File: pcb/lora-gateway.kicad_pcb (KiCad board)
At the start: 2 copper layers, 78.3 x 25.8 mm, 22 parts, among them J1 USB_B_Micro, J2 Conn_01x06, J3 Conn_01x06, J4 Conn_Coaxial, J5 AVR-JTAG-10, J6 AVR-ISP-6, SW1 SW_Push, U1 RFM95W-868S2, U2 ATmega2560-16A, U3 LM1117-3.3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

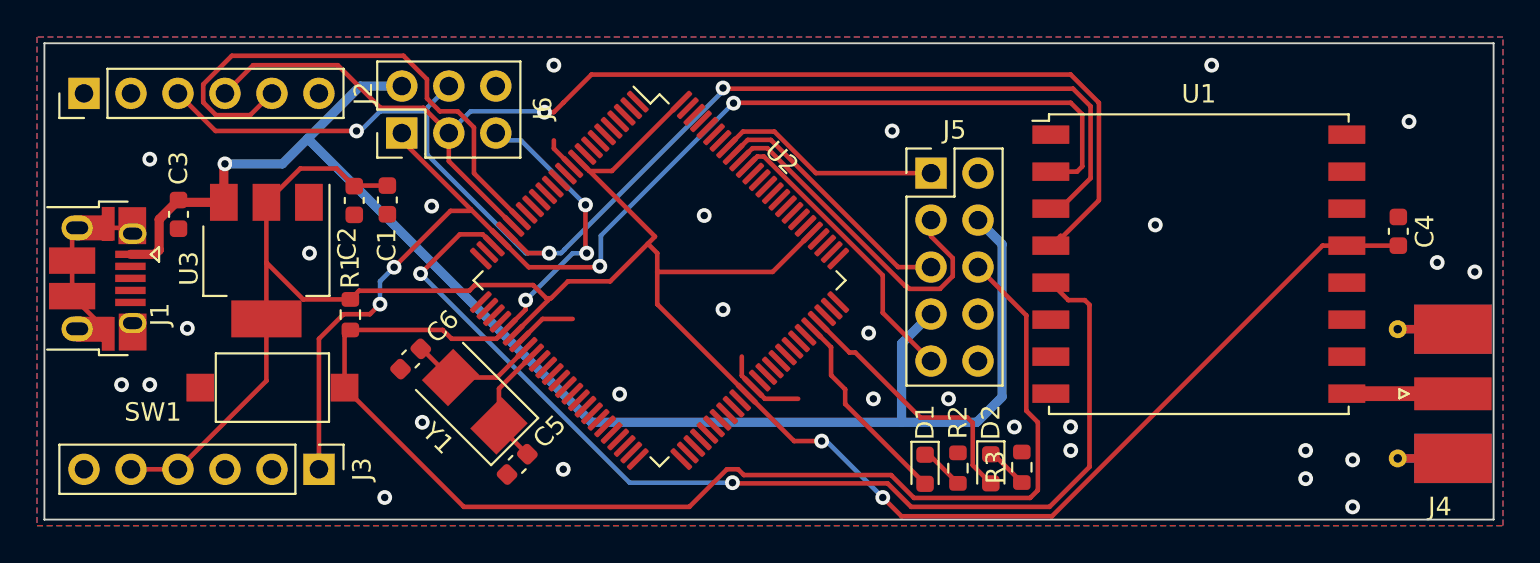
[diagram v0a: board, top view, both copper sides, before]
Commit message: add rfm95 wiring
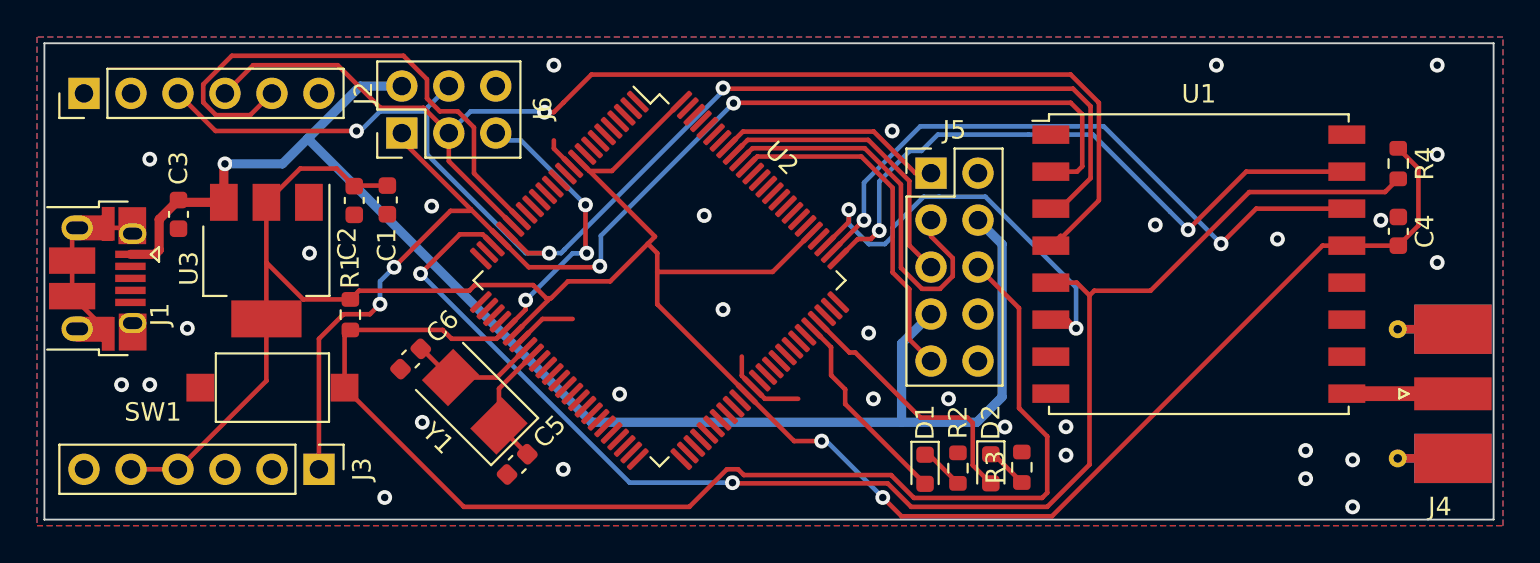
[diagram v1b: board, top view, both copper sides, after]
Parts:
- added R4: R_Small, Resistor_SMD:R_0603_1608Metric, F.Cu at (111.7, 64.8)
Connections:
- U1 pad 14: unconnected-(U1-DIO0-Pad14) -> DIO0
- U1 pad 15: unconnected-(U1-DIO1-Pad15) -> DIO1
- U2 pad 76: unconnected-(U2-PA2-Pad76) -> DIO1
- U2 pad 77: unconnected-(U2-PA1-Pad77) -> DIO0
- U2 pad 78: unconnected-(U2-PA0-Pad78) -> RST_LORA
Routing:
- net DIO0: track 0.00 -> 35.3 mm, vias 0 -> 2
- net DIO1: track 0.00 -> 35.3 mm, vias 0 -> 2
- net RST_LORA: track 0.00 -> 23.1 mm, vias 0 -> 2
- net SS_LORA: track 58.7 -> 78.2 mm
- net +3V3: track 129.2 -> 135.4 mm
- net TDI: track 16.0 -> 19.0 mm
- net TDO: track 18.7 -> 21.4 mm
- net TMS: track 13.8 -> 15.9 mm
- net RST: track 82.7 -> 83.5 mm
- net GND: vias 29 -> 31

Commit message: add gnd to micro usb
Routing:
- net GND: track 9.80 -> 12.2 mm
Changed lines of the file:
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@@
   (segment (start 66.04 63.939645) (end 66.04 63.5) (width 0.25) (layer "F.Cu") (net 11))
   (segment (start 64.213584 74.363853) (end 65.425437 73.152) (width 0.25) (layer "F.Cu") (net 11))
+  (segment (start 43.15 72.26) (end 45.336 72.26) (width 0.5) (layer "F.Cu") (net 11))
   (segment (start 76.2 76.220965) (end 76.2 75.184) (width 0.25) (layer "F.Cu") (net 11))
   (segment (start 77.449035 77.47) (end 79.248 77.47) (width 0.25) (layer "F.Cu") (net 11))
   (segment (start 76.817762 76.838727) (end 77.449035 77.47) (width 0.25) (layer "F.Cu") (net 11))
+  (segment (start 45.336 72.26) (end 45.466 72.39) (width 0.5) (layer "F.Cu") (net 11))
   (segment (start 67.042011 64.941656) (end 66.04 63.939645) (width 0.25) (layer "F.Cu") (net 11))
   (via (at 83.058 73.914) (size 0.8) (drill 0.4) (layers "F.Cu" "B.Cu") (free) (net 11))
